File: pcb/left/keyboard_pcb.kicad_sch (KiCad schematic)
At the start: 108 parts, among them J1 Alt. Battery, J2 Alt. Switch, K00 KEYSW, K01 KEYSW, K02 KEYSW, K03 KEYSW, K04 KEYSW, K05 KEYSW, K10 KEYSW, K11 KEYSW, K12 KEYSW, K13 KEYSW, K14 KEYSW, K15 KEYSW, K20 KEYSW, K21 KEYSW, K22 KEYSW, K23 KEYSW, K24 KEYSW, K25 KEYSW, K33 KEYSW, K34 KEYSW, K35 KEYSW, U1 Flippable RP2040 ProMicro/nic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

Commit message: Base slide switch on KiCad library version
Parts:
- 右S1, 左S1: footprint ♥Project_Library:SW_MSK12C02-HB_Mirrorable -> ♥Project_Library:SW_SPDT_PCM12_Reversible
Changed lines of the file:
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@@
       (effects (font (size 1.27 1.27)) hide)
     )
-    (property "Footprint" "♥Project_Library:SW_MSK12C02-HB_Mirrorable" (at 48.26 127 0)
+    (property "Footprint" "♥Project_Library:SW_SPDT_PCM12_Reversible" (at 48.26 127 0)
       (effects (font (size 1.27 1.27)) hide)
     )
@@
       (effects (font (size 1.27 1.27)) hide)
     )
-    (property "Footprint" "♥Project_Library:SW_MSK12C02-HB_Mirrorable" (at 48.26 99.06 0)
-      (effects (font (size 1.27 1.27)) hide)
-    )
+    (property "Footprint" "♥Project_Library:SW_SPDT_PCM12_Reversible" (at 48.26 99.06 0)
+      (effects (font (size 1.27 1.27)) hide)
+    )

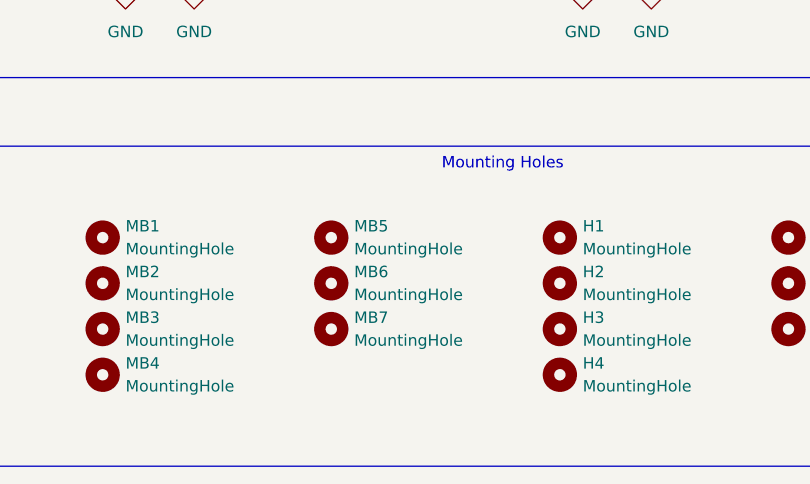
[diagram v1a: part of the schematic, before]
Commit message: Assign reset button footprint and remove unneeded mouse-bite symbols
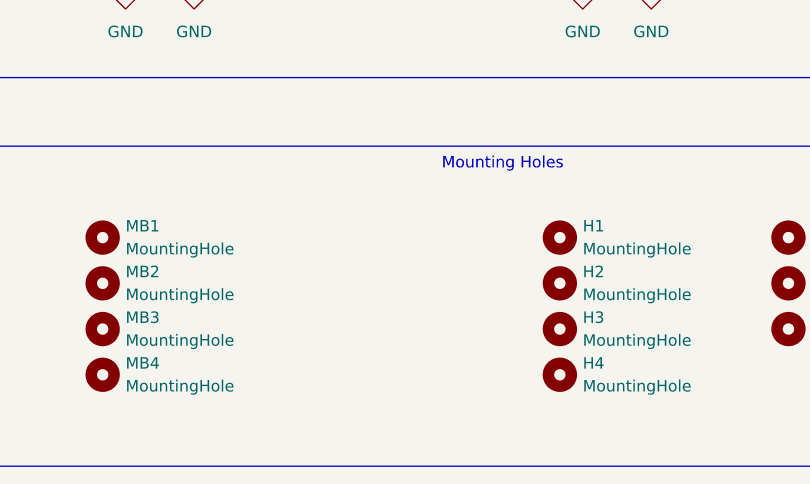
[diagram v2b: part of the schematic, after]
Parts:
- removed MB5, MB6, MB7: MountingHole, beekeeb_lib:mousebites, symbol Mechanical:MountingHole
- 右S2, 左S2: footprint (none) -> Button_Switch_SMD:SW_SPST_TL3342
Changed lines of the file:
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@@
-    )
-  )
-  (symbol (lib_id "Mechanical:MountingHole") (at 55.88 251.46 0) (unit 1)
-    (in_bom yes) (on_board yes) (dnp no)
-    (property "Reference" "MB5" (at 58.42 250.1899 0)
-      (effects (font (size 1.27 1.27)) (justify left))
-    )
-    (property "Value" "MountingHole" (at 58.42 252.7299 0)
-      (effects (font (size 1.27 1.27)) (justify left))
-    )
-    (property "Footprint" "beekeeb_lib:mousebites" (at 55.88 251.46 0)
-      (effects (font (size 1.27 1.27)) hide)
-    )
-    (property "Datasheet" "~" (at 55.88 251.46 0)
-      (effects (font (size 1.27 1.27)) hide)
-    )
-    (instances
-      (project "keyboard_pcb"
-        (path "/9538e4ed-27e6-4c37-b989-9859dc0d49e8"
-          (reference "MB5") (unit 1)
-        )
-      )
     )
   )
@@
       (effects (font (size 1.27 1.27)))
     )
-    (property "Footprint" "" (at 48.26 149.86 0)
+    (property "Footprint" "Button_Switch_SMD:SW_SPST_TL3342" (at 48.26 149.86 0)
       (effects (font (size 1.27 1.27)) hide)
     )
@@
         (path "/9538e4ed-27e6-4c37-b989-9859dc0d49e8"
           (reference "#PWR05") (unit 1)
-        )
-      )
-    )
-  )
-  (symbol (lib_id "Mechanical:MountingHole") (at 55.88 261.62 0) (unit 1)
-    (in_bom yes) (on_board yes) (dnp no)
-    (property "Reference" "MB7" (at 58.42 260.3499 0)
-      (effects (font (size 1.27 1.27)) (justify left))
-    )
-    (property "Value" "MountingHole" (at 58.42 262.8899 0)
-      (effects (font (size 1.27 1.27)) (justify left))
-    )
-    (property "Footprint" "beekeeb_lib:mousebites" (at 55.88 261.62 0)
-      (effects (font (size 1.27 1.27)) hide)
-    )
-    (property "Datasheet" "~" (at 55.88 261.62 0)
-      (effects (font (size 1.27 1.27)) hide)
-    )
-    (instances
-      (project "keyboard_pcb"
-        (path "/9538e4ed-27e6-4c37-b989-9859dc0d49e8"
-          (reference "MB7") (unit 1)
         )
       )
@@
     )
   )
-  (symbol (lib_id "Mechanical:MountingHole") (at 55.88 256.54 0) (unit 1)
-    (in_bom yes) (on_board yes) (dnp no)
-    (property "Reference" "MB6" (at 58.42 255.2699 0)
-      (effects (font (size 1.27 1.27)) (justify left))
-    )
-    (property "Value" "MountingHole" (at 58.42 257.8099 0)
-      (effects (font (size 1.27 1.27)) (justify left))
-    )
-    (property "Footprint" "beekeeb_lib:mousebites" (at 55.88 256.54 0)
-      (effects (font (size 1.27 1.27)) hide)
-    )
-    (property "Datasheet" "~" (at 55.88 256.54 0)
-      (effects (font (size 1.27 1.27)) hide)
-    )
-    (instances
-      (project "keyboard_pcb"
-        (path "/9538e4ed-27e6-4c37-b989-9859dc0d49e8"
-          (reference "MB6") (unit 1)
-        )
-      )
-    )
-  )
   (symbol (lib_id "Device:D") (at 320.04 113.03 90) (unit 1)
     (in_bom yes) (on_board yes) (dnp no)
@@
       (effects (font (size 1.27 1.27)))
     )
-    (property "Footprint" "" (at 48.26 165.1 0)
-      (effects (font (size 1.27 1.27)) hide)
-    )
+    (property "Footprint" "Button_Switch_SMD:SW_SPST_TL3342" (at 48.26 165.1 0)
+      (effects (font (size 1.27 1.27)) hide)
+    )

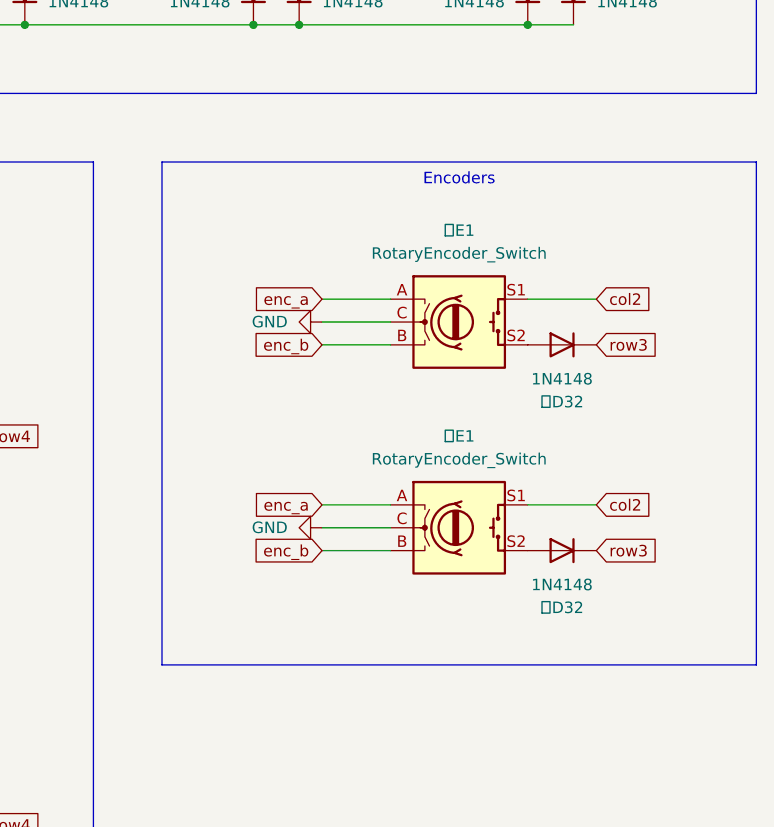
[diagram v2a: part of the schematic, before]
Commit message: Change roller encoder to reversible version
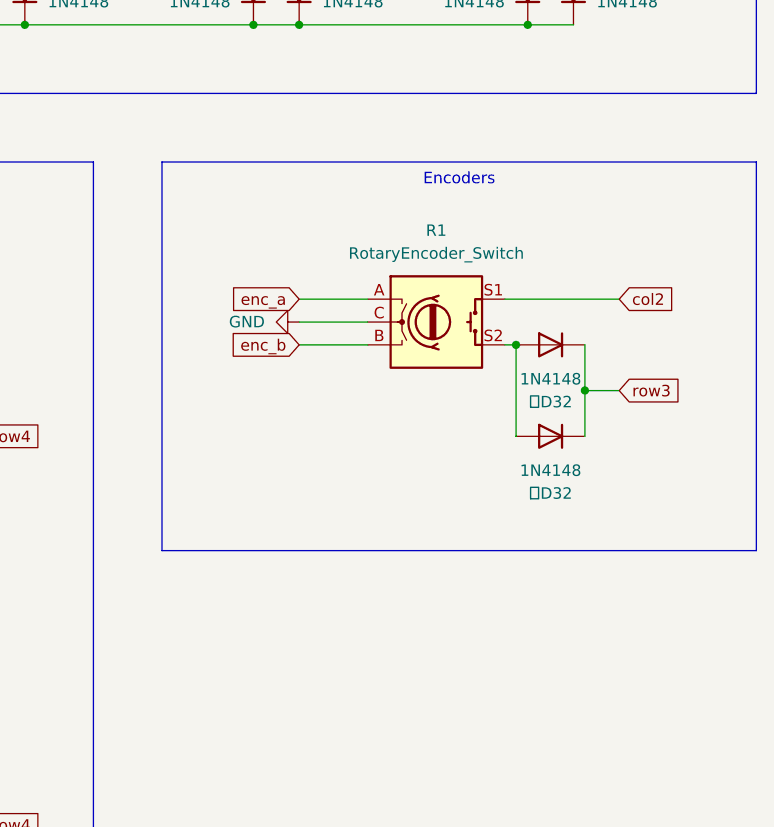
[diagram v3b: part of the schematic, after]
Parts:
- removed 右E1: RotaryEncoder_Switch, ♥Project_Library:RollerEncoder_Panasonic_EVQWGD001, symbol Device:RotaryEncoder_Switch
- renumbered 左E1 to R1
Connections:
- net at R1.S2, 左D32.2 (A): now also 右D32.2 (A)
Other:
- moved on the sheet: R1, 左D32

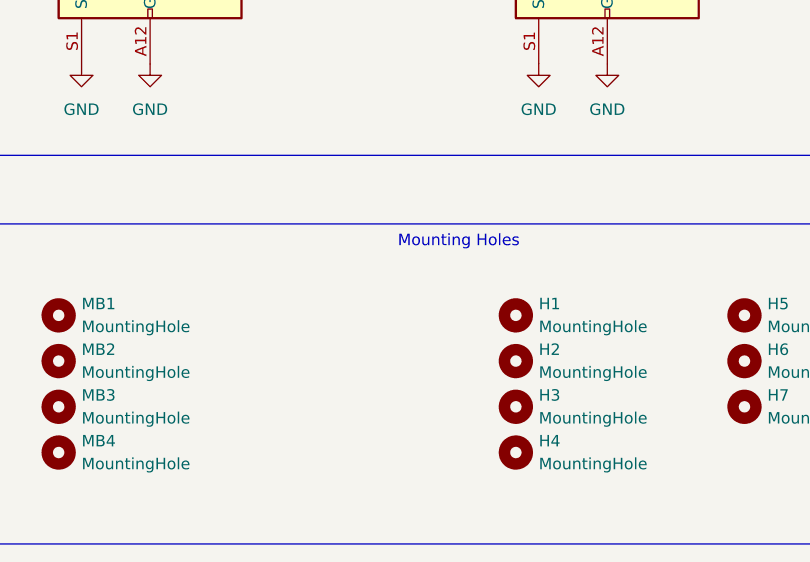
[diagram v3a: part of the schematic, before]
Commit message: Add battery cut-out
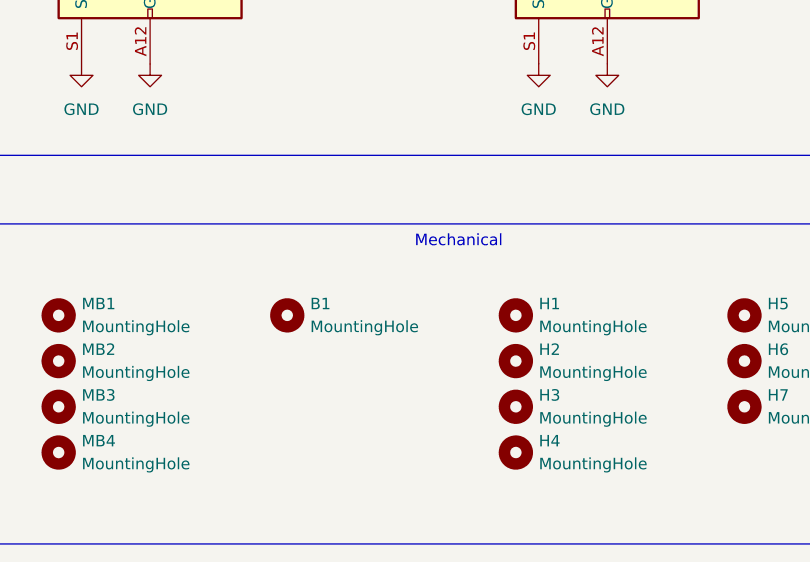
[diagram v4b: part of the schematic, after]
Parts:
- added B1: MountingHole, beekeeb_lib:mousebites, symbol Mechanical:MountingHole
- R1: footprint ♥Project_Library:RollerEncoder_Panasonic_EVQWGD001 -> ♥Project_Library:RollerEncoder_Panasonic_EVQWGD001_Reversible
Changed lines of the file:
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@@
     (effects (font (size 1.27 1.27)) (justify top))
   )
-  (text_box "Mounting Holes"
+  (text_box "Mechanical"
     (at 17.78 241.3 0) (size 114.3 35.56)
     (stroke (width 0) (type default))
@@
     )
   )
+  (symbol (lib_id "Mechanical:MountingHole") (at 55.88 251.46 0) (unit 1)
+    (in_bom yes) (on_board yes) (dnp no) (fields_autoplaced)
+    (property "Reference" "B1" (at 58.42 250.19 0)
+      (effects (font (size 1.27 1.27)) (justify left))
+    )
+    (property "Value" "MountingHole" (at 58.42 252.73 0)
+      (effects (font (size 1.27 1.27)) (justify left))
+    )
+    (property "Footprint" "beekeeb_lib:mousebites" (at 55.88 251.46 0)
+      (effects (font (size 1.27 1.27)) hide)
+    )
+    (property "Datasheet" "~" (at 55.88 251.46 0)
+      (effects (font (size 1.27 1.27)) hide)
+    )
+    (instances
+      (project "keyboard_pcb"
+        (path "/9538e4ed-27e6-4c37-b989-9859dc0d49e8"
+          (reference "B1") (unit 1)
+        )
+      )
+    )
+  )
   (symbol (lib_id "Switch:SW_Push") (at 264.16 127 0) (unit 1)
     (in_bom yes) (on_board yes) (dnp no)
@@
       (effects (font (size 1.27 1.27)))
     )
-    (property "Footprint" "♥Project_Library:RollerEncoder_Panasonic_EVQWGD001" (at 300.99 199.136 0)
+    (property "Footprint" "♥Project_Library:RollerEncoder_Panasonic_EVQWGD001_Reversible" (at 300.99 199.136 0)
       (effects (font (size 1.27 1.27)) hide)
     )

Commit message: Tweak footprint for USB socket
That location on the board will either have the mid-mount USB socket (wired boards) or the power switch (wireless boards). Since the mid-mount socket requires a cut-out but the switch does not, the socket cut-out is made optional using mouse-bites.
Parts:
- 右J2, 左J2: footprint ♥Project_Library:CUI_UJC-HP-L-G-5-MSMT-TR -> ♥Project_Library:CUI_UJC-HP-L-G-5-MSMT-TR_Reversible_Optional
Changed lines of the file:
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@@
       (effects (font (size 1.27 1.27)))
     )
-    (property "Footprint" "♥Project_Library:CUI_UJC-HP-L-G-5-MSMT-TR" (at 95.25 203.2 0)
+    (property "Footprint" "♥Project_Library:CUI_UJC-HP-L-G-5-MSMT-TR_Reversible_Optional" (at 95.25 203.2 0)
       (effects (font (size 1.27 1.27)) hide)
     )
@@
       (effects (font (size 1.27 1.27)))
     )
-    (property "Footprint" "♥Project_Library:CUI_UJC-HP-L-G-5-MSMT-TR" (at 44.45 203.2 0)
-      (effects (font (size 1.27 1.27)) hide)
-    )
+    (property "Footprint" "♥Project_Library:CUI_UJC-HP-L-G-5-MSMT-TR_Reversible_Optional" (at 44.45 203.2 0)
+      (effects (font (size 1.27 1.27)) hide)
+    )

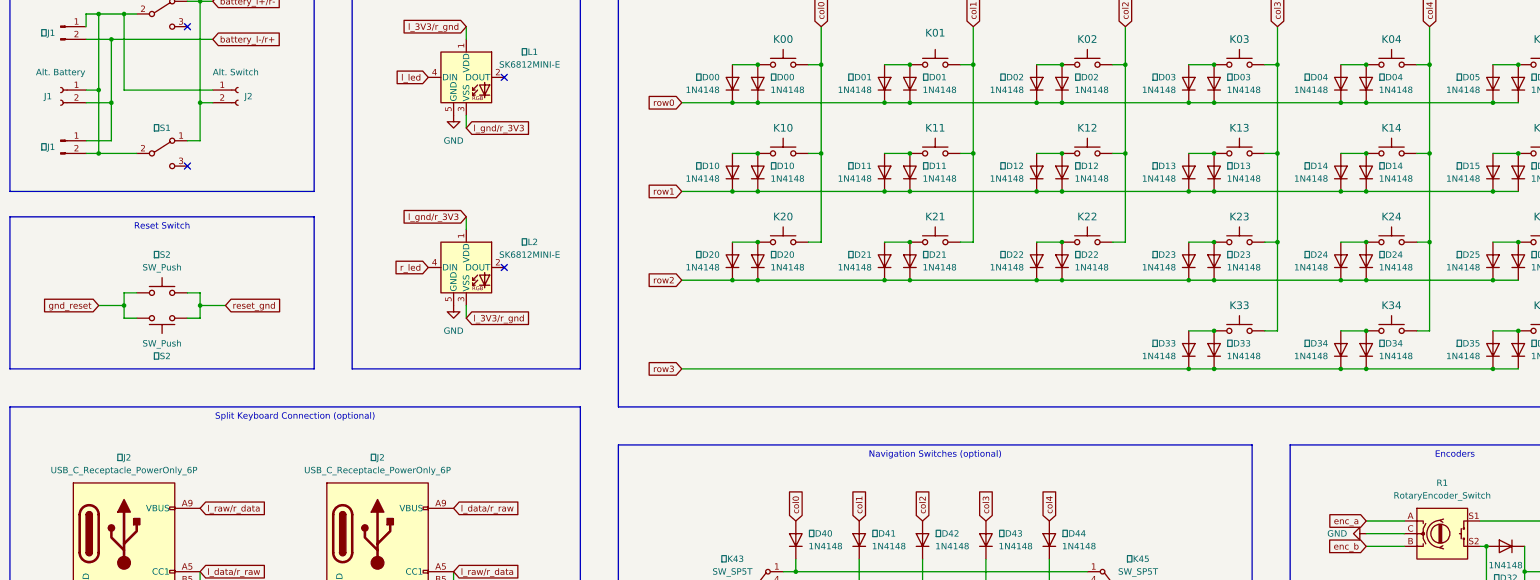
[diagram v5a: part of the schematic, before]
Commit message: Fix minor issues and footprint assignments
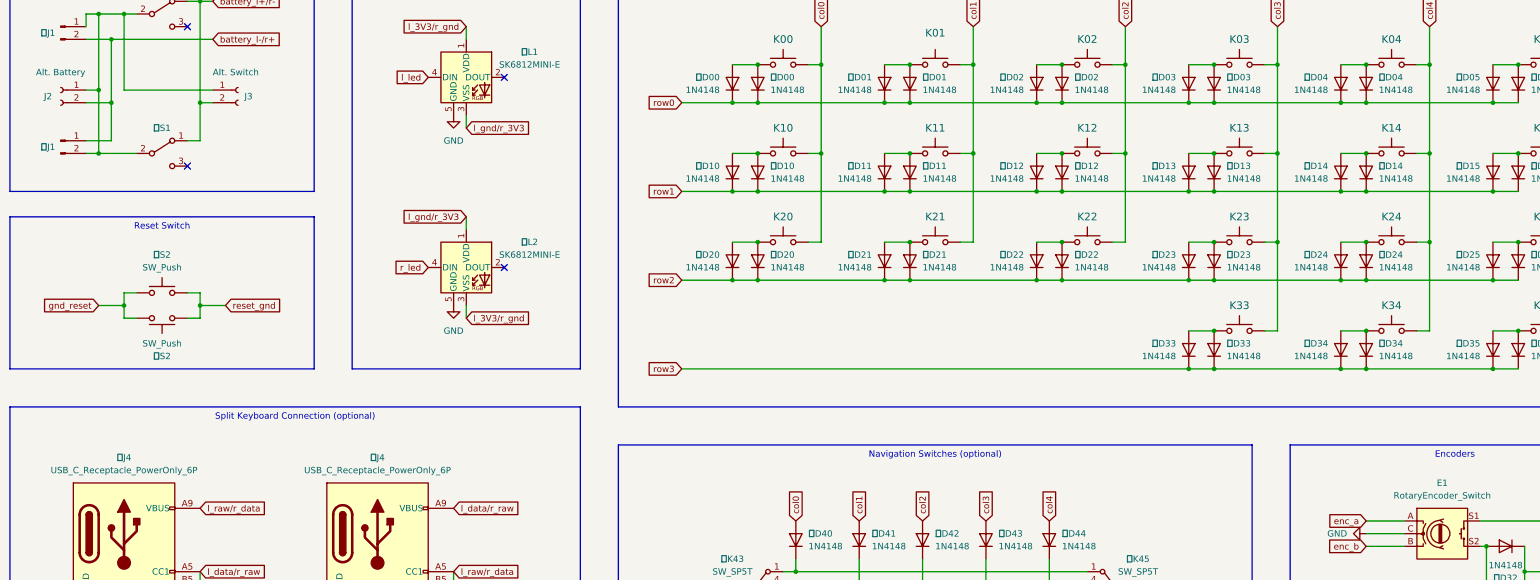
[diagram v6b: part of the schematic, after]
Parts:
- B1: footprint beekeeb_lib:mousebites -> ♥Project_Library:Battery_Cutout_401020
- 右L2, 左L1: footprint LED_SMD:LED_SK6812MINI_PLCC4_3.5x3.5mm_P1.75mm -> ♥Project_Library:SK6812-MINI-E_Jumped_GND
- renumbered R1 to E1, J1 to J2, J2 to J3, 右J2 to 右J4, 左J2 to 左J4
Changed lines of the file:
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@@
       (effects (font (size 1.27 1.27)))
     )
-    (property "Footprint" "LED_SMD:LED_SK6812MINI_PLCC4_3.5x3.5mm_P1.75mm" (at 110.49 157.48 0)
+    (property "Footprint" "♥Project_Library:SK6812-MINI-E_Jumped_GND" (at 110.49 157.48 0)
       (effects (font (size 1.27 1.27)) (justify left top) hide)
     )
@@
   (symbol (lib_id "Connector:USB_C_Receptacle_PowerOnly_6P") (at 91.44 205.74 0) (unit 1)
     (in_bom yes) (on_board yes) (dnp no) (fields_autoplaced)
-    (property "Reference" "右J2" (at 91.44 187.96 0)
+    (property "Reference" "右J4" (at 91.44 187.96 0)
       (effects (font (size 1.27 1.27)))
     )
@@
       (project "keyboard_pcb"
         (path "/9538e4ed-27e6-4c37-b989-9859dc0d49e8"
-          (reference "右J2") (unit 1)
+          (reference "右J4") (unit 1)
         )
       )
@@
   (symbol (lib_id "Connector:Conn_01x02_Socket") (at 27.94 114.3 0) (mirror y) (unit 1)
     (in_bom yes) (on_board yes) (dnp no)
-    (property "Reference" "J1" (at 25.4 115.57 0)
+    (property "Reference" "J2" (at 25.4 115.57 0)
       (effects (font (size 1.27 1.27)))
     )
@@
       (project "keyboard_pcb"
         (path "/9538e4ed-27e6-4c37-b989-9859dc0d49e8"
-          (reference "J1") (unit 1)
+          (reference "J2") (unit 1)
         )
       )
@@
   (symbol (lib_id "Connector:Conn_01x02_Socket") (at 63.5 114.3 0) (unit 1)
     (in_bom yes) (on_board yes) (dnp no)
-    (property "Reference" "J2" (at 64.77 115.57 0)
+    (property "Reference" "J3" (at 64.77 115.57 0)
       (effects (font (size 1.27 1.27)) (justify left))
     )
@@
       (project "keyboard_pcb"
         (path "/9538e4ed-27e6-4c37-b989-9859dc0d49e8"
-          (reference "J2") (unit 1)
+          (reference "J3") (unit 1)
         )
       )
@@
       (effects (font (size 1.27 1.27)))
     )
-    (property "Footprint" "LED_SMD:LED_SK6812MINI_PLCC4_3.5x3.5mm_P1.75mm" (at 110.49 119.38 0)
+    (property "Footprint" "♥Project_Library:SK6812-MINI-E_Jumped_GND" (at 110.49 119.38 0)
       (effects (font (size 1.27 1.27)) (justify left top) hide)
     )
@@
       (effects (font (size 1.27 1.27)) (justify left))
     )
-    (property "Footprint" "beekeeb_lib:mousebites" (at 55.88 251.46 0)
+    (property "Footprint" "♥Project_Library:Battery_Cutout_401020" (at 55.88 251.46 0)
       (effects (font (size 1.27 1.27)) hide)
     )
@@
   (symbol (lib_id "Connector:USB_C_Receptacle_PowerOnly_6P") (at 40.64 205.74 0) (unit 1)
     (in_bom yes) (on_board yes) (dnp no) (fields_autoplaced)
-    (property "Reference" "左J2" (at 40.64 187.96 0)
+    (property "Reference" "左J4" (at 40.64 187.96 0)
       (effects (font (size 1.27 1.27)))
     )
@@
       (project "keyboard_pcb"
         (path "/9538e4ed-27e6-4c37-b989-9859dc0d49e8"
-          (reference "左J2") (unit 1)
+          (reference "左J4") (unit 1)
         )
       )
@@
   (symbol (lib_id "Device:RotaryEncoder_Switch") (at 304.8 203.2 0) (unit 1)
     (in_bom yes) (on_board yes) (dnp no)
-    (property "Reference" "R1" (at 304.8 193.04 0)
+    (property "Reference" "E1" (at 304.8 193.04 0)
       (effects (font (size 1.27 1.27)))
     )
@@
       (project "keyboard_pcb"
         (path "/9538e4ed-27e6-4c37-b989-9859dc0d49e8"
-          (reference "R1") (unit 1)
-        )
-      )
+          (reference "E1") (unit 1)
+        )
+      )
